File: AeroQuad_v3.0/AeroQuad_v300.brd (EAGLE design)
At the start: 89.8 x 55.9 mm, 65 parts, among them U1 MPU-6000, U10 MS5611, U9 HMC5883LSMD, X1 06FLZ-SM1

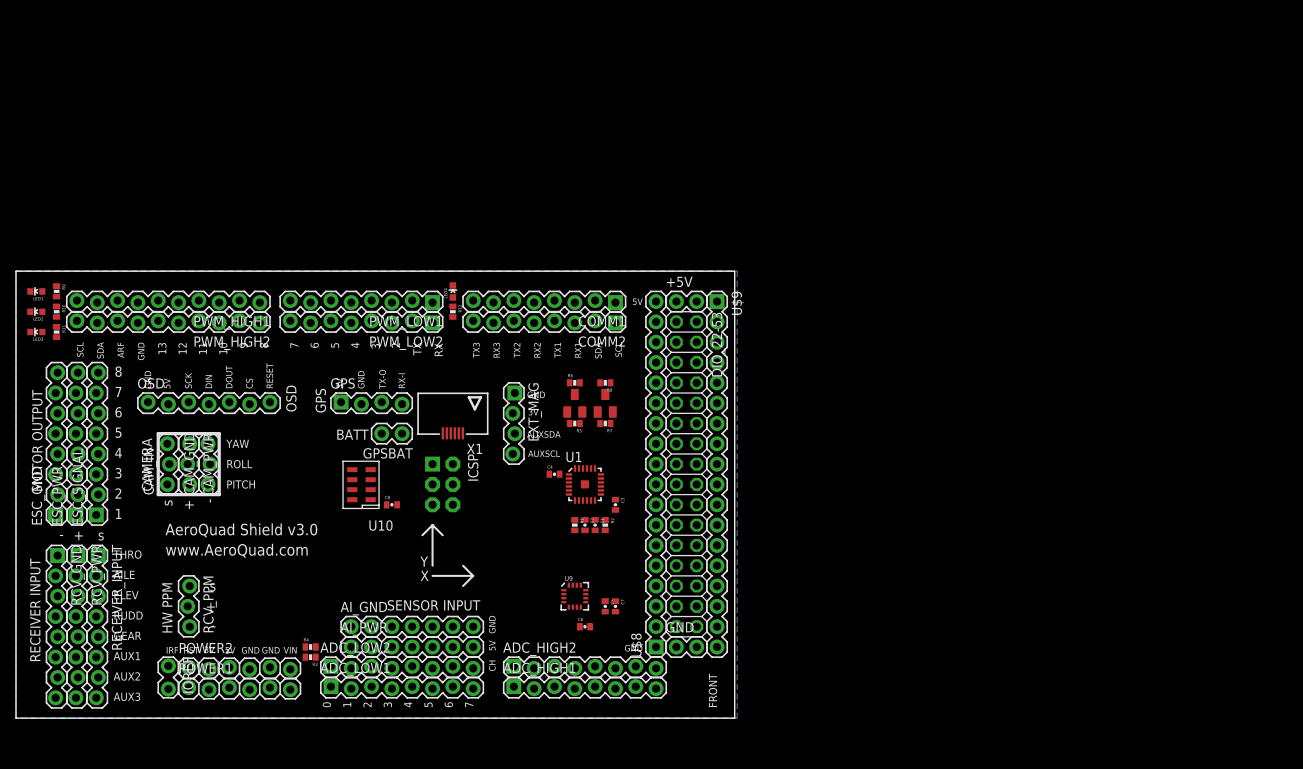
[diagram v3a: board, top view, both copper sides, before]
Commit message: Begin work on Due compatible AQ shield
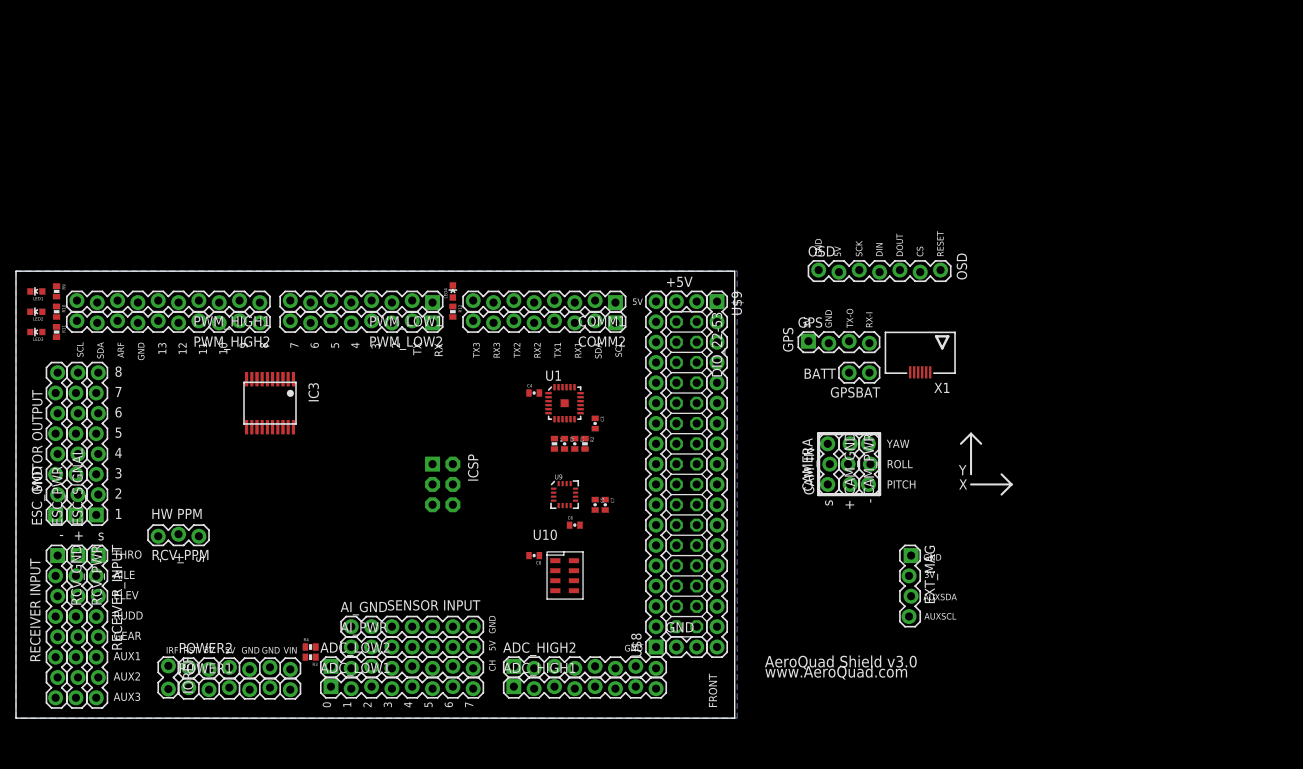
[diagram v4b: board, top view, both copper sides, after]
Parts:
- removed R5, R6, R7, R8: 10k, SparkFun:0402-RES
- removed U$1, U$2: BSS138, ava:BSS138
- added IC3: 74245MTC, adafruit:SSOP20
- moved OSD 85.4 mm to (100.3, 55.9)
- moved CAM_GND 82.6 mm to (106.7, 29.2)
- moved CAM_IN 82.5 mm to (101.6, 29.2)
- moved CAM_PWR 82.5 mm to (104.1, 34.3)
- moved GPSBAT 58.9 mm to (106.7, 43.2)
- moved GPS 58.9 mm to (99.1, 47.0)
- moved X1 58.9 mm to (113.0, 45.7)
- moved EXT_MAG 53.5 mm to (111.8, 20.3)
- moved U10 27.9 mm to (68.6, 17.8), turned to 0 degrees
- moved C8 18.9 mm to (64.8, 20.3), turned to 180 degrees
- moved C7 12.8 mm to (73.7, 26.7)
- moved C6 12.8 mm to (69.8, 24.1)
- moved C5 12.8 mm to (72.4, 26.7)
- moved U9 12.8 mm to (68.6, 27.9)
- moved C1 10.5 mm to (69.8, 34.3)
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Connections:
- removed net CAM_PITCH: CAM_IN.1, PWM_HIGH1.4, PWM_HIGH2.4
- removed net CAM_ROLL: CAM_IN.2, PWM_HIGH1.5, PWM_HIGH2.5
- removed net HWPPM: DIO_22-53.27, RCV_PPM.1, U$8.4
- removed net N$16: ESC_SIGNAL.3, PWM_LOW1.6, PWM_LOW2.6
- removed net N$21: ESC_SIGNAL.1, PWM_LOW1.3, PWM_LOW2.3
- removed net N$23: ESC_SIGNAL.4, PWM_LOW1.7, PWM_LOW2.7
- removed net N$24: ESC_SIGNAL.5, PWM_LOW1.8, PWM_LOW2.8
- removed net N$25: ESC_SIGNAL.6, PWM_HIGH1.1, PWM_HIGH2.1
- removed net N$26: ESC_SIGNAL.7, PWM_HIGH1.2, PWM_HIGH2.2
- removed net N$27: ESC_SIGNAL.8, PWM_HIGH1.3, PWM_HIGH2.3
- removed net SCL: COMM1.1, COMM2.1, R8.1, U$2.D
- removed net SDA: COMM1.2, COMM2.2, R6.1, U$1.D
- removed net SERVO2: DIO_22-53.13, U$8.11
- removed net SERVO4: DIO_22-53.15, U$8.10
- removed net SERVO6: DIO_22-53.17, U$8.9
- removed net SERVO8: DIO_22-53.19, U$8.8
- new net PWM10: IC3.6, PWM_HIGH1.3, PWM_HIGH2.3
- new net PWM11: IC3.7, PWM_HIGH1.4, PWM_HIGH2.4
- new net PWM12: IC3.8, PWM_HIGH1.5, PWM_HIGH2.5
- new net PWM13: IC3.9, PWM_HIGH1.6, PWM_HIGH2.6
- new net PWM2: IC3.2, PWM_LOW1.3, PWM_LOW2.3
- new net PWM3: IC3.3, PWM_LOW1.4, PWM_LOW2.4
- new net PWM34: DIO_22-53.13, ESC_SIGNAL.4, U$8.11
- new net PWM36: DIO_22-53.15, ESC_SIGNAL.3, U$8.10
- new net PWM38: DIO_22-53.17, ESC_SIGNAL.2, U$8.9
- new net PWM4: IC3.4, PWM_LOW1.5, PWM_LOW2.5
- new net PWM40: DIO_22-53.19, ESC_SIGNAL.1, U$8.8
- new net PWM5: IC3.5, PWM_LOW1.6, PWM_LOW2.6
- new net PWM6: ESC_SIGNAL.5, PWM_LOW1.7, PWM_LOW2.7
- new net PWM7: ESC_SIGNAL.6, PWM_LOW1.8, PWM_LOW2.8
- new net PWM8: ESC_SIGNAL.7, PWM_HIGH1.1, PWM_HIGH2.1
- new net PWM9: ESC_SIGNAL.8, PWM_HIGH1.2, PWM_HIGH2.2
- net 3.3V: now also IC3.20; no longer R5.2, R7.2, U$1.G, U$2.G
- net 5V: no longer R6.2, R8.2
- net AILE: now also IC3.12; no longer ADC_HIGH1.2, ADC_HIGH2.2
- net AUX1: now also IC3.16; no longer ADC_HIGH1.6, ADC_HIGH2.6
- net AUX2: now also IC3.17; no longer ADC_HIGH1.7, ADC_HIGH2.7
- net AUX3: now also IC3.18; no longer ADC_HIGH1.8, ADC_HIGH2.8
- net ELEV: now also IC3.13; no longer ADC_HIGH1.3, ADC_HIGH2.3
- net GEAR: now also IC3.15; no longer ADC_HIGH1.5, ADC_HIGH2.5
- net GND: now also IC3.1, IC3.10, IC3.19
- net N$5: now also DIO_22-53.27, U$8.4; no longer ESC_SIGNAL.2, PWM_LOW1.4, PWM_LOW2.4
- net RDY2_LED: no longer PWM_LOW1.5, PWM_LOW2.5
- net RDY_LED: no longer CAM_IN.3, PWM_HIGH1.6, PWM_HIGH2.6
- net RUDD: now also IC3.14; no longer ADC_HIGH1.4, ADC_HIGH2.4
- net SCL-L: now also COMM1.1, COMM2.1; no longer R7.1, U$2.S
- net SDA-L: now also COMM1.2, COMM2.2; no longer R5.1, U$1.S
- net THRO: now also IC3.11, RCV_PPM.1; no longer ADC_HIGH1.1, ADC_HIGH2.1

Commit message: added camera servo pins, starting overall review of other Due pins
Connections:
- net SCL1 renamed SCL1-L
- net SDA1 renamed SDA1-L
- removed net LED2: DIO_22-53.23, U$8.6
- removed net SERVO10: DIO_22-53.21, U$8.7
- removed net SS: DIO_22-53.32, U$9.17
- new net CAM1: CAM_IN.1, DIO_22-53.21, U$8.7
- new net CAM2: CAM_IN.2, DIO_22-53.23, U$8.6
- new net CAM3: CAM_IN.3, DIO_22-53.32, U$9.17
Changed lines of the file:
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@@
 <wire x1="85.09" y1="24.13" x2="87.63" y2="24.13" width="0" layer="19" extent="1-1"/>
 </signal>
-<signal name="LED2">
+<signal name="CAM2">
 <contactref element="DIO_22-53" pad="23"/>
 <contactref element="U$8" pad="6"/>
+<contactref element="CAM_IN" pad="2"/>
+<wire x1="82.55" y1="21.59" x2="101.727" y2="31.75" width="0" layer="19" extent="1-1"/>
 <wire x1="80.01" y1="21.59" x2="82.55" y2="21.59" width="0" layer="19" extent="1-1"/>
 </signal>
@@
 <wire x1="85.09" y1="26.67" x2="87.63" y2="26.67" width="0" layer="19" extent="1-1"/>
 </signal>
-<signal name="SERVO10">
+<signal name="CAM1">
 <contactref element="DIO_22-53" pad="21"/>
 <contactref element="U$8" pad="7"/>
+<contactref element="CAM_IN" pad="1"/>
+<wire x1="82.55" y1="24.13" x2="101.473" y2="29.21" width="0" layer="19" extent="1-1"/>
 <wire x1="80.01" y1="24.13" x2="82.55" y2="24.13" width="0" layer="19" extent="1-1"/>
 </signal>
-<signal name="SS">
+<signal name="CAM3">
 <contactref element="DIO_22-53" pad="32"/>
 <contactref element="U$9" pad="17"/>
+<contactref element="CAM_IN" pad="3"/>
+<wire x1="87.63" y1="11.43" x2="101.473" y2="34.29" width="0" layer="19" extent="1-1"/>
 <wire x1="85.09" y1="11.43" x2="87.63" y2="11.43" width="0" layer="19" extent="1-1"/>
 </signal>
@@
 <wire x1="69.83" y1="37.37" x2="85.09" y2="46.99" width="0" layer="19" extent="1-1"/>
 </signal>
-<signal name="SDA1">
+<signal name="SDA1-L">
 <contactref element="PWM_HIGH1" pad="9"/>
 <contactref element="PWM_HIGH2" pad="9"/>
 <wire x1="10.16" y1="49.403" x2="10.16" y2="51.943" width="0" layer="19" extent="1-1"/>
 </signal>
-<signal name="SCL1">
+<signal name="SCL1-L">
 <contactref element="PWM_HIGH1" pad="10"/>
 <contactref element="PWM_HIGH2" pad="10"/>
